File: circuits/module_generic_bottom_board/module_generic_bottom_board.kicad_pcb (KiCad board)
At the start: 2 copper layers, 24.1 x 77.5 mm, 7 parts, among them P1 CONN_02X05, P2 CONN_02X05, P3 CONN_01X11, P4 CONN_01X01, P5 CONN_01X01

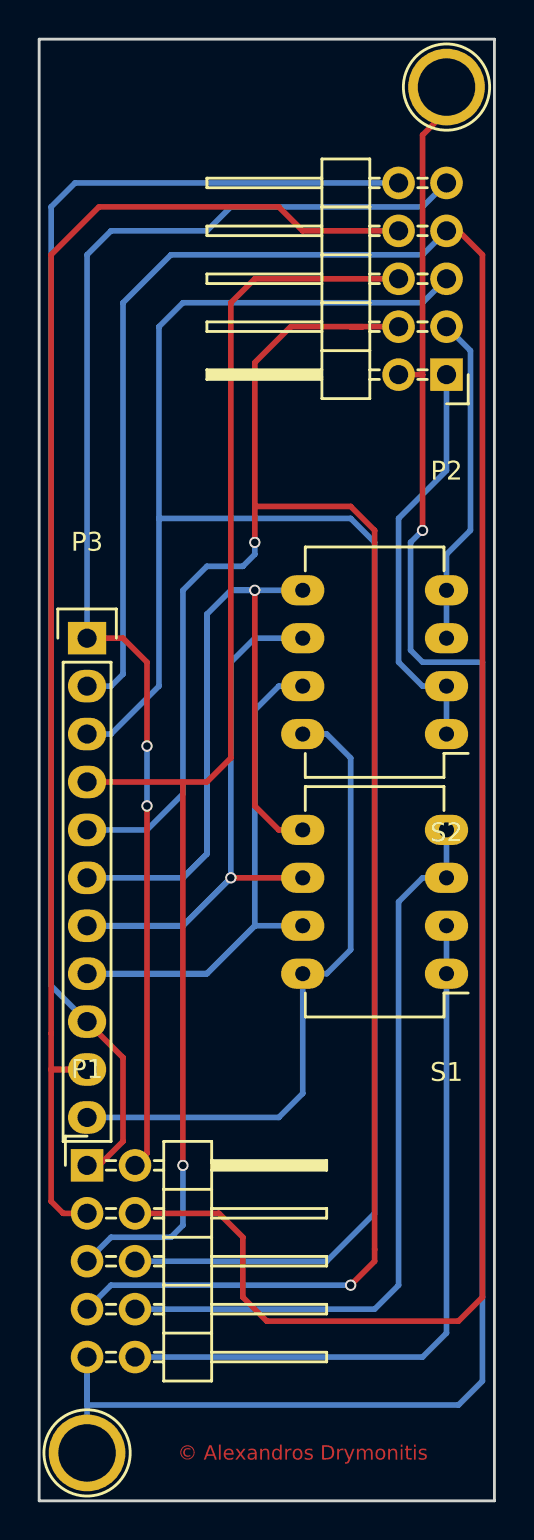
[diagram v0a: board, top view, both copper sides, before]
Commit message: Update module_generic_bottom_board
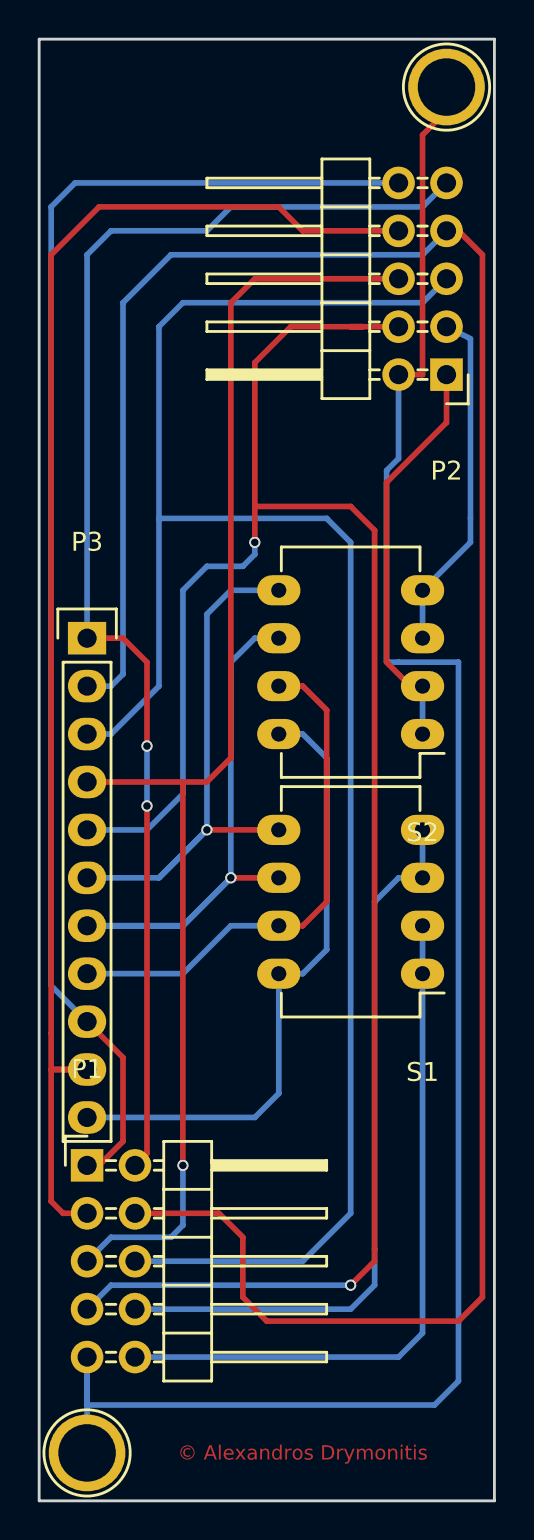
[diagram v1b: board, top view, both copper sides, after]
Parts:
- moved S1 1.27 mm to (154.9, 132.1)
- moved S2 1.27 mm to (154.9, 119.4)
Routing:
- net /SHIFTIN_SER: track 55.4 -> 30.6 mm
- net /QH/: track 36.9 -> 27.5 mm
- net /QH: track 36.9 -> 34.4 mm
- net /MUXA: track 101.5 -> 98.9 mm
- net /SW1_12: track 38.6 -> 37.4 mm
- net /SW1_34: track 40.4 -> 39.2 mm
- net /SHIFTOUT_SER: track 34.6 -> 33.3 mm
- net GND: track 103.2 -> 102.3 mm, vias 1 -> 0
- net /SW2_34: track 17.6 -> 18.3 mm
